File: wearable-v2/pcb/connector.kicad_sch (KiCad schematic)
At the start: 35 parts, among them J1 HERALD_V2_CONN_RECEPTACLE, J11 PNL_1, J12 PNL_2, J13 PNL_3, J14 PNL_4, J2 HERALD_V2_CONN_RECEPTACLE, J3 HERALD_V2_CONN_RECEPTACLE, J4 HERALD_V2_CONN_RECEPTACLE, J7 USB_C_Receptacle_USB2.0, U1 DT1446-04V, U15 TLV751, U2 MCP73831/2-2MC, U3 TCA6408A, U4 FT201XQ

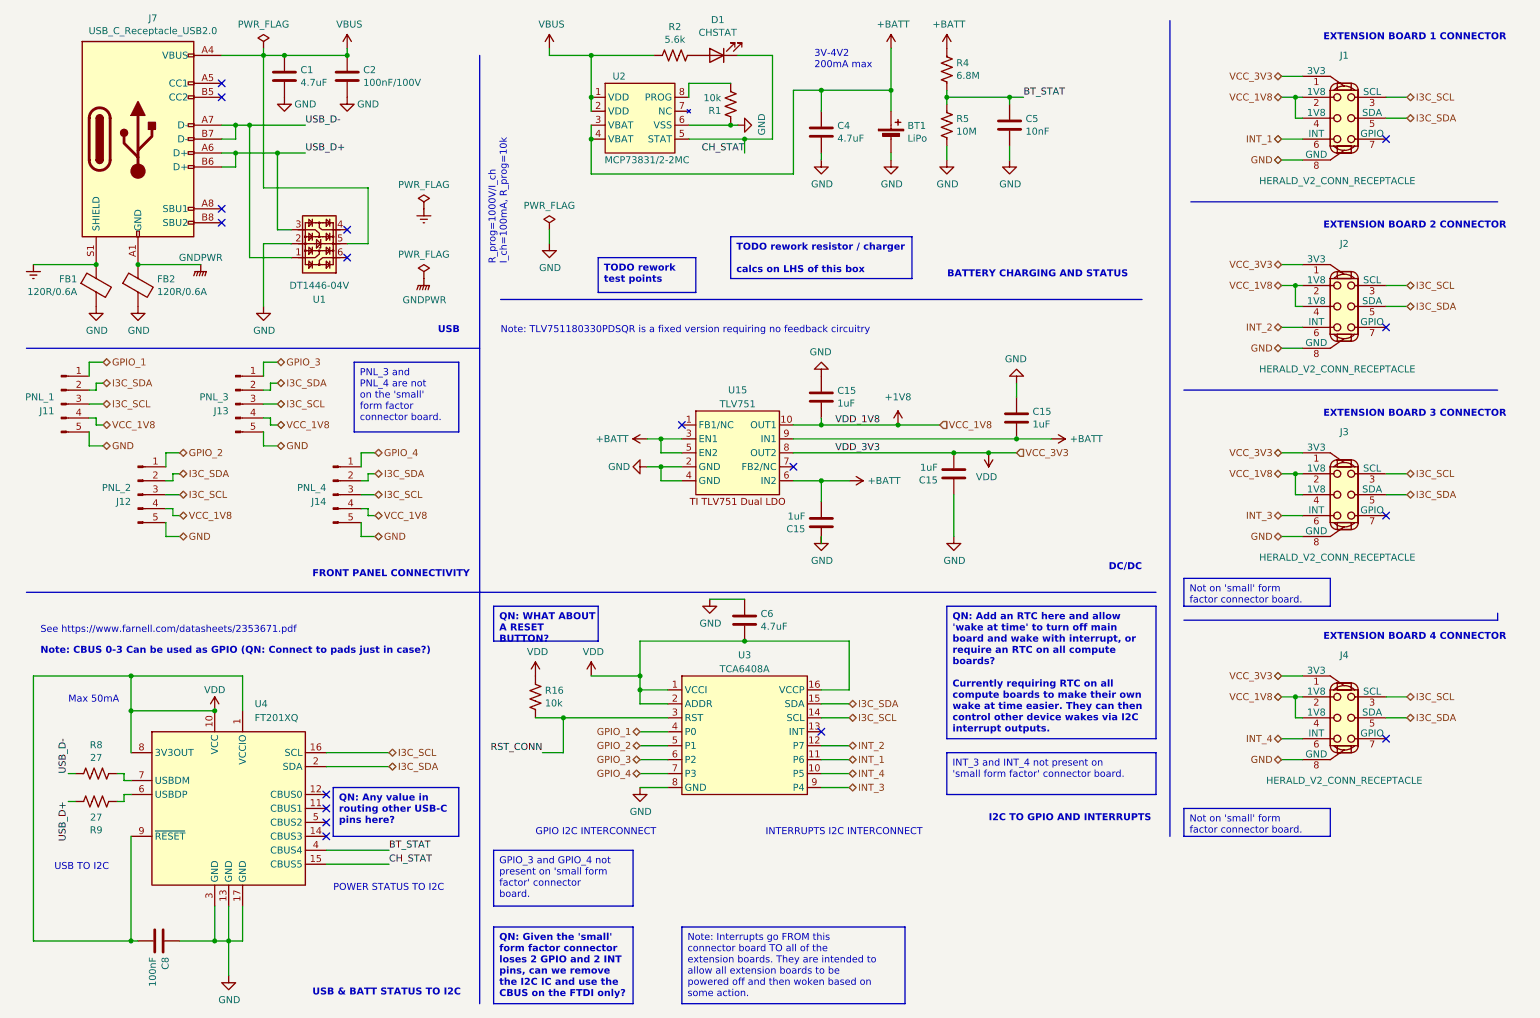
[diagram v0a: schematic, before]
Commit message: Added I2C and I3C notes and additional resistors
Signed-off-by: Adam Fowler <adam@adamfowler.org>
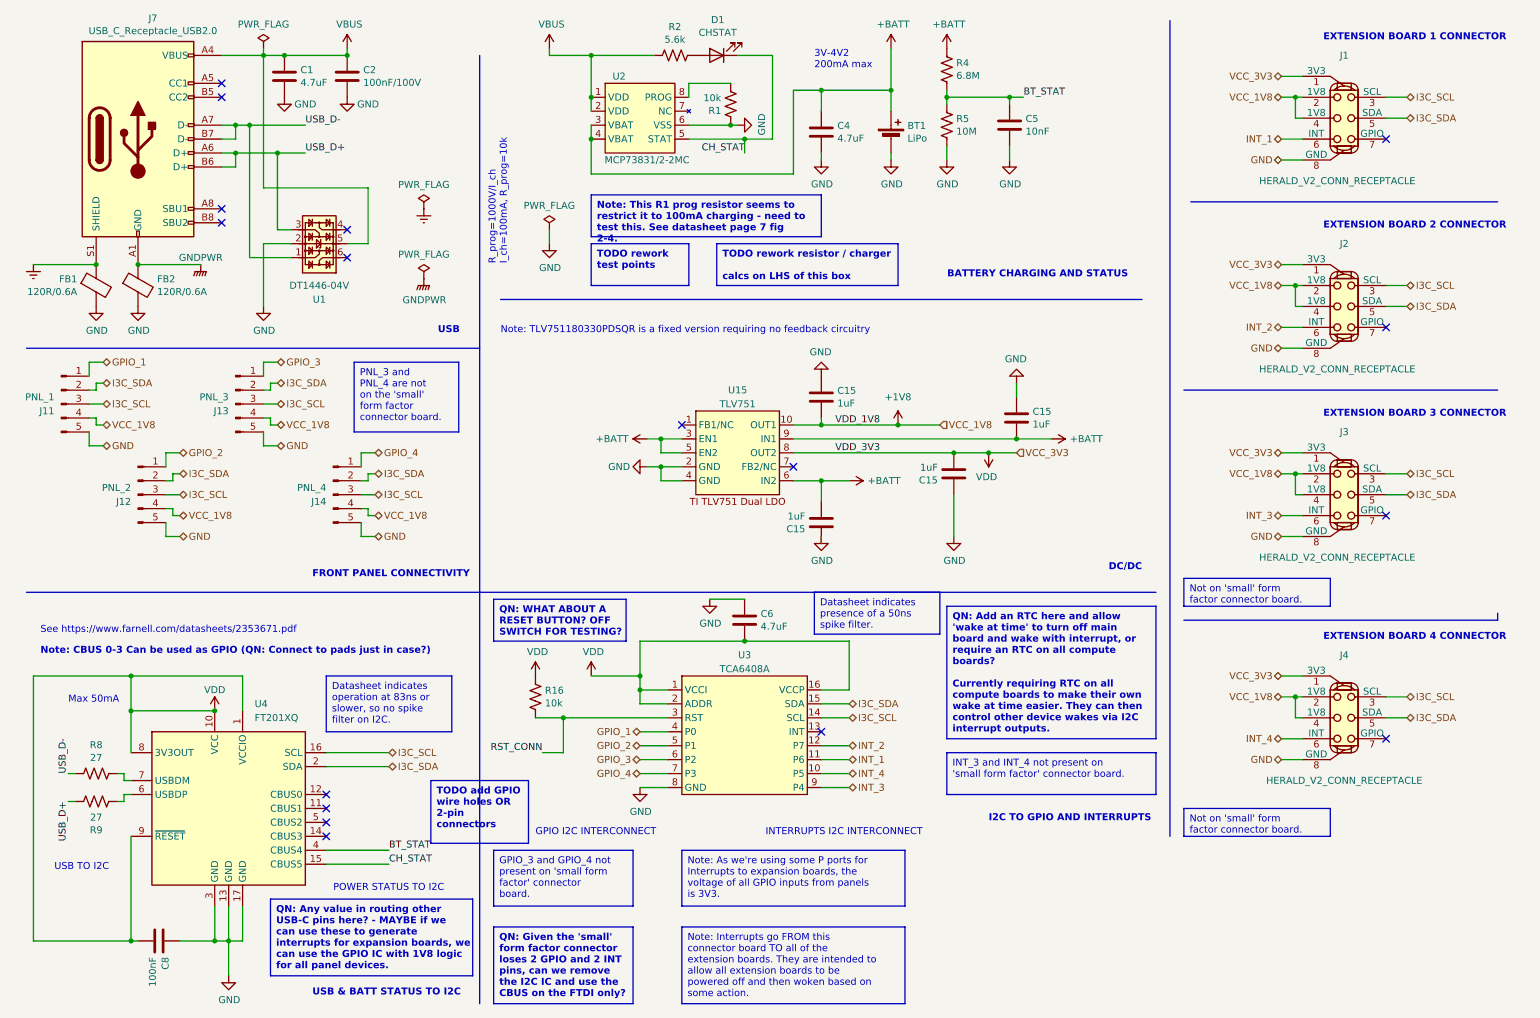
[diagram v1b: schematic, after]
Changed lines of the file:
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@@
     (effects (font (size 1.27 1.27)) (justify left top))
   )
-  (text_box "QN: Any value in routing other USB-C pins here?"
-    (at 69.85 154.94 0) (size 22.86 8.89)
+  (text_box "Datasheet indicates operation at 83ns or slower, so no spike filter on I2C."
+    (at 68.58 134.62 0) (size 22.86 10.16)
+    (stroke (width 0) (type default))
+    (fill (type none))
+    (effects (font (size 1.27 1.27)) (justify left top))
+  )
+  (text_box "QN: Any value in routing other USB-C pins here? - MAYBE if we can use these to generate interrupts for expansion boards, we can use the GPIO IC with 1V8 logic for all panel devices."
+    (at 58.42 175.26 0) (size 36.83 13.97)
     (stroke (width 0) (type default))
     (fill (type none))
@@
   )
   (text_box "TODO rework test points"
-    (at 118.11 58.42 0) (size 17.78 6.35)
+    (at 116.84 55.88 0) (size 17.78 7.62)
     (stroke (width 0) (type default))
     (fill (type none))
@@
     (effects (font (size 1.27 1.27)) (justify left top))
   )
-  (text_box "QN: WHAT ABOUT A RESET BUTTON?"
-    (at 99.06 121.92 0) (size 19.05 6.35)
+  (text_box "TODO add GPIO wire holes OR 2-pin connectors"
+    (at 87.63 153.67 0) (size 17.78 11.43)
     (stroke (width 0) (type default))
     (fill (type none))
     (effects (font (size 1.27 1.27) bold) (justify left top))
+  )
+  (text_box "Note: This R1 prog resistor seems to restrict it to 100mA charging - need to test this. See datasheet page 7 fig 2-4."
+    (at 116.84 46.99 0) (size 41.91 7.62)
+    (stroke (width 0) (type default))
+    (fill (type none))
+    (effects (font (size 1.27 1.27) bold) (justify left top))
+  )
+  (text_box "Note: As we're using some P ports for Interrupts to expansion boards, the voltage of all GPIO inputs from panels is 3V3."
+    (at 133.35 166.37 0) (size 40.64 10.16)
+    (stroke (width 0) (type default))
+    (fill (type none))
+    (effects (font (size 1.27 1.27)) (justify left top))
+  )
+  (text_box "QN: WHAT ABOUT A RESET BUTTON? OFF SWITCH FOR TESTING?"
+    (at 99.06 120.65 0) (size 24.13 7.62)
+    (stroke (width 0) (type default))
+    (fill (type none))
+    (effects (font (size 1.27 1.27) bold) (justify left top))
+  )
+  (text_box "Datasheet indicates presence of a 50ns spike filter."
+    (at 157.48 119.38 0) (size 22.86 7.62)
+    (stroke (width 0) (type default))
+    (fill (type none))
+    (effects (font (size 1.27 1.27)) (justify left top))
   )
   (text_box "INT_3 and INT_4 not present on 'small form factor' connector board."
@@
   )
   (text_box "TODO rework resistor / charger \ncalcs on LHS of this box"
-    (at 142.24 54.61 0) (size 33.02 7.62)
+    (at 139.7 55.88 0) (size 33.02 7.62)
     (stroke (width 0) (type default))
     (fill (type none))
